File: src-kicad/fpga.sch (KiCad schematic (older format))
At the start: 1 part

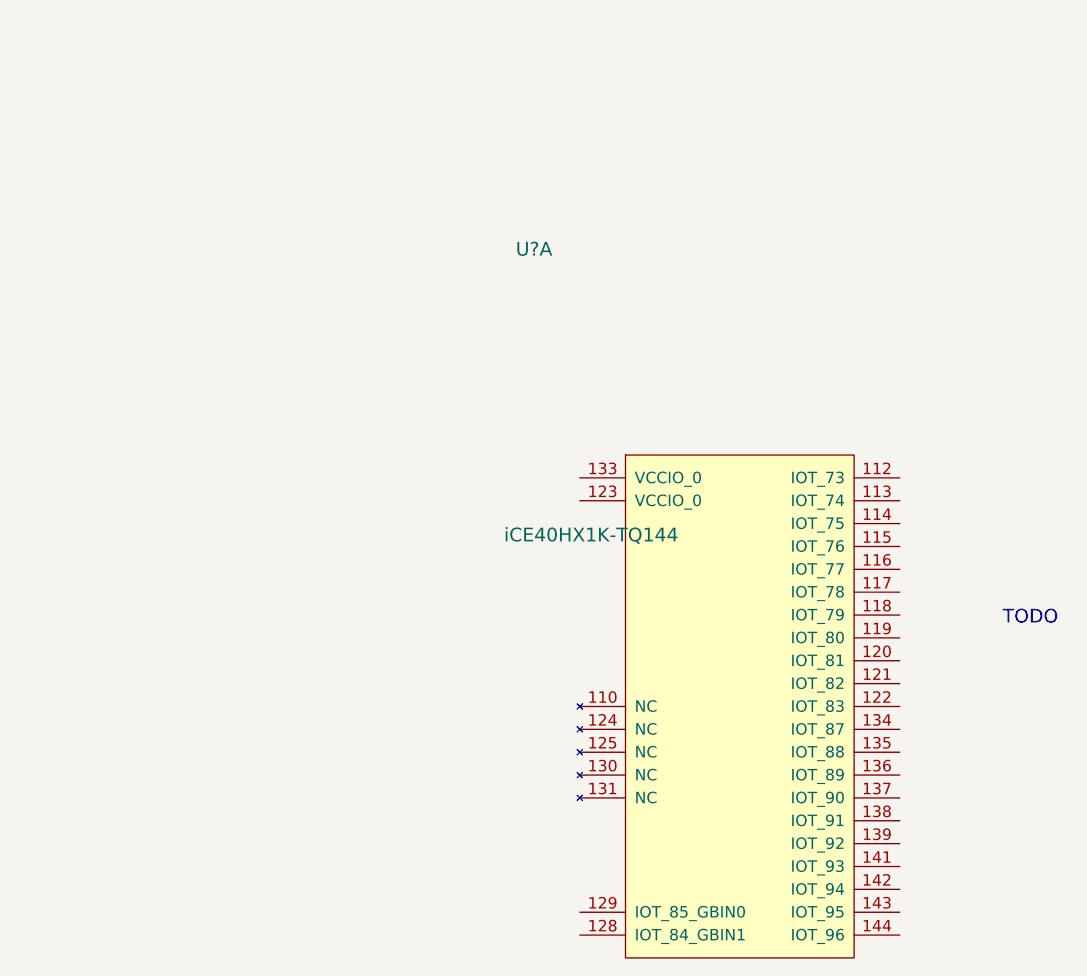
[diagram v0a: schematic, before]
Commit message: Kicad migration: component FPGA bank0 done
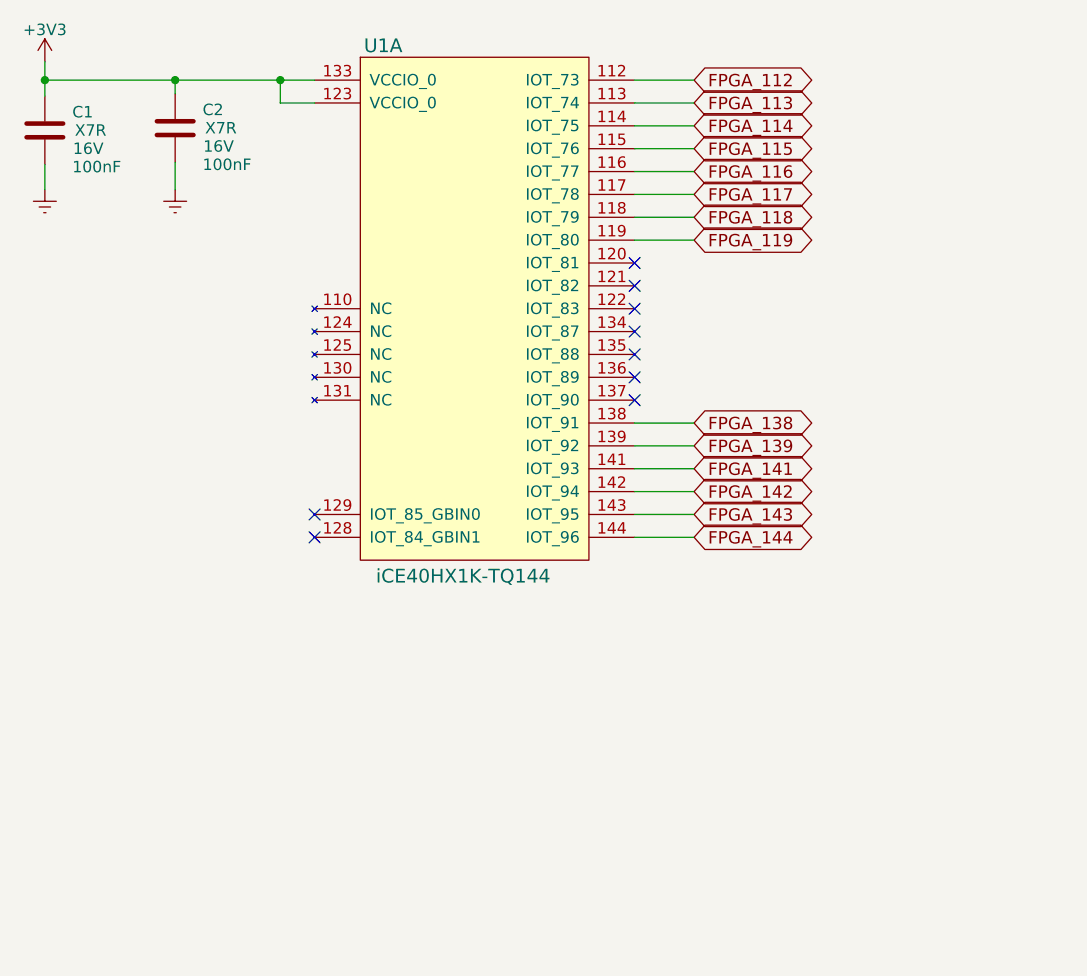
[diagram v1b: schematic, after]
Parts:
- removed U?: iCE40HX1K-TQ144, symbol iCE40HX1K-TQ144
- added C1, C2: 100nF, symbol C
- added U1: iCE40HX1K-TQ144, symbol iCE40HX1K-TQ144
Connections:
- new net +3V3: C1.1, C2.1, U1.123 (VCCIO_0), U1.133 (VCCIO_0)
- new net FPGA_112: U1.112 (IOT_73)
- new net FPGA_113: U1.113 (IOT_74)
- new net FPGA_114: U1.114 (IOT_75)
- new net FPGA_115: U1.115 (IOT_76)
- new net FPGA_116: U1.116 (IOT_77)
- new net FPGA_117: U1.117 (IOT_78)
- new net FPGA_118: U1.118 (IOT_79)
- new net FPGA_119: U1.119 (IOT_80)
- new net FPGA_138: U1.138 (IOT_91)
- new net FPGA_139: U1.139 (IOT_92)
- new net FPGA_141: U1.141 (IOT_93)
- new net FPGA_142: U1.142 (IOT_94)
- new net FPGA_143: U1.143 (IOT_95)
- new net FPGA_144: U1.144 (IOT_96)
- new net GNDREF: C1.2, C2.2
- no-connect marks 0 -> 9
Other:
- note removed: "TODO"
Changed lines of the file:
@@
 encoding utf-8
 Sheet 2 2
-Title ""
-Date ""
+Title "Icezum Alhambra"
+Date "2016-05-23"
 Rev ""
 Comp ""
@@
 Comment4 ""
 $EndDescr
-Text Notes 5150 3400 0    60   ~ 0
-TODO
 $Comp
-L iCE40HX1K-TQ144 U?
-U 1 1 5742AF05
-P 3300 2750
-F 0 "U?" H 3100 3750 60  0000 C CNN
-F 1 "iCE40HX1K-TQ144" H 3350 2500 60  0000 C CNN
-F 2 "" H 3300 2750 60  0000 C CNN
-F 3 "" H 3300 2750 60  0000 C CNN
-	1    3300 2750
+L iCE40HX1K-TQ144 U1
+U 1 1 5742DE36
+P 2140 1010
+F 0 "U1" H 2440 1160 60  0000 C CNN
+F 1 "iCE40HX1K-TQ144" H 2790 -1160 60  0000 C CNN
+F 2 "" H 2440 610 60  0000 C CNN
+F 3 "" H 2440 610 60  0000 C CNN
+	1    2140 1010
 	1    0    0    -1
 $EndComp
+$Comp
+L C C1
+U 1 1 5742E2A9
+P 960 1230
+F 0 "C1" H 1080 1310 50  0000 L CNN
+F 1 "100nF" H 1080 1070 50  0000 L CNN
+F 2 "" H 998 1080 50  0000 C CNN
+F 3 "" H 960 1230 50  0000 C CNN
+F 4 "X7R" H 1160 1230 50  0000 C CNN "class"
+F 5 "16V" H 1150 1150 50  0000 C CNN "Voltage"
+	1    960  1230
+	1    0    0    -1
+$EndComp
+$Comp
+L +3V3 #PWR?
+U 1 1 5742EB21
+P 960 930
+F 0 "#PWR?" H 960 780 50  0001 C CNN
+F 1 "+3V3" H 960 1070 50  0000 C CNN
+F 2 "" H 960 930 50  0000 C CNN
+F 3 "" H 960 930 50  0000 C CNN
+	1    960  930
+	1    0    0    -1
+$EndComp
+Wire Wire Line
+	960  930  960  1080
+$Comp
+L GNDREF #PWR?
+U 1 1 5742F120
+P 960 1490
+F 0 "#PWR?" H 960 1240 50  0001 C CNN
+F 1 "GNDREF" H 960 1340 50  0001 C CNN
+F 2 "" H 960 1490 50  0000 C CNN
+F 3 "" H 960 1490 50  0000 C CNN
+	1    960  1490
+	1    0    0    -1
+$EndComp
+Wire Wire Line
+	960  1490 960  1380
+$Comp
+L C C2
+U 1 1 5742F27A
+P 1530 1220
+F 0 "C2" H 1650 1300 50  0000 L CNN
+F 1 "100nF" H 1650 1060 50  0000 L CNN
+F 2 "" H 1568 1070 50  0000 C CNN
+F 3 "" H 1530 1220 50  0000 C CNN
+F 4 "X7R" H 1730 1220 50  0000 C CNN "class"
+F 5 "16V" H 1720 1140 50  0000 C CNN "Voltage"
+	1    1530 1220
+	1    0    0    -1
+$EndComp
+$Comp
+L GNDREF #PWR?
+U 1 1 5742F317
+P 1530 1490
+F 0 "#PWR?" H 1530 1240 50  0001 C CNN
+F 1 "GNDREF" H 1530 1340 50  0001 C CNN
+F 2 "" H 1530 1490 50  0000 C CNN
+F 3 "" H 1530 1490 50  0000 C CNN
+	1    1530 1490
+	1    0    0    -1
+$EndComp
+Wire Wire Line
+	1530 1370 1530 1490
+Wire Wire Line
+	960  1010 2140 1010
+Connection ~ 960  1010
+Wire Wire Line
+	1530 1070 1530 1010
+Connection ~ 1530 1010
+Wire Wire Line
+	2140 1110 1990 1110
+Wire Wire Line
+	1990 1110 1990 1010
+Connection ~ 1990 1010
+NoConn ~ 2140 2910
+NoConn ~ 2140 3010
+Wire Wire Line
+	3540 1010 3800 1010
+Text GLabel 3800 1010 2    54   BiDi ~ 0
+FPGA_112
+Text GLabel 3800 1110 2    54   BiDi ~ 0
+FPGA_113
+Wire Wire Line
+	3540 1110 3800 1110
+Text GLabel 3800 1210 2    54   BiDi ~ 0
+FPGA_114
+Text GLabel 3800 1310 2    54   BiDi ~ 0
+FPGA_115
+Text GLabel 3800 1410 2    54   BiDi ~ 0
+FPGA_116
+Text GLabel 3800 1510 2    54   BiDi ~ 0
+FPGA_117
+Text GLabel 3800 1610 2    54   BiDi ~ 0
+FPGA_118
+Text GLabel 3800 1710 2    54   BiDi ~ 0
+FPGA_119
+Wire Wire Line
+	3540 1210 3800 1210
+Wire Wire Line
+	3800 1310 3540 1310
+Wire Wire Line
+	3540 1410 3800 1410
+Wire Wire Line
+	3800 1510 3540 1510
+Wire Wire Line
+	3540 1610 3800 1610
+Wire Wire Line
+	3800 1710 3540 1710
+Text GLabel 3800 2510 2    54   BiDi ~ 0
+FPGA_138
+Text GLabel 3800 2610 2    54   BiDi ~ 0
+FPGA_139
+Text GLabel 3800 2710 2    54   BiDi ~ 0
+FPGA_141
+Text GLabel 3800 2810 2    54   BiDi ~ 0
+FPGA_142
+Text GLabel 3800 2910 2    54   BiDi ~ 0
+FPGA_143
+Text GLabel 3800 3010 2    54   BiDi ~ 0
+FPGA_144
+Wire Wire Line
+	3540 3010 3800 3010
+Wire Wire Line
+	3800 2910 3540 2910
+Wire Wire Line
+	3540 2810 3800 2810
+Wire Wire Line
+	3800 2710 3540 2710
+Wire Wire Line
+	3540 2610 3800 2610
+Wire Wire Line
+	3540 2510 3800 2510
+NoConn ~ 3540 1810
+NoConn ~ 3540 1910
+NoConn ~ 3540 2010
+NoConn ~ 3540 2110
+NoConn ~ 3540 2210
+NoConn ~ 3540 2310
+NoConn ~ 3540 2410
 $EndSCHEMATC

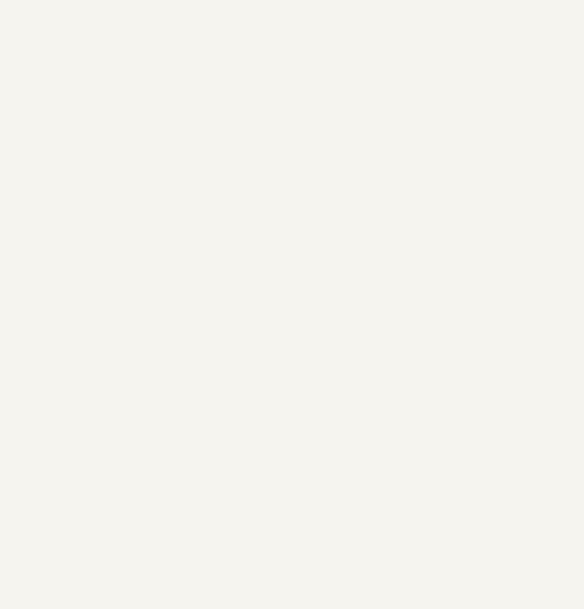
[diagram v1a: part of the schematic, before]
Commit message: Kicad. FPGA: bank 1 component created
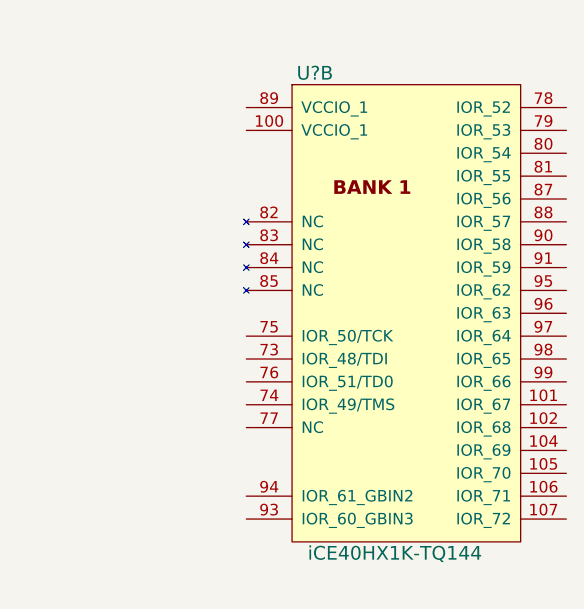
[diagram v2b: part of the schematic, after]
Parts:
- added U?: iCE40HX1K-TQ144, symbol iCE40HX1K-TQ144
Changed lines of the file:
@@
 NoConn ~ 3540 2310
 NoConn ~ 3540 2410
+$Comp
+L iCE40HX1K-TQ144 U?
+U 2 1 57436BD0
+P 5700 1130
+F 0 "U?" H 6000 1280 60  0000 C CNN
+F 1 "iCE40HX1K-TQ144" H 6350 -820 60  0000 C CNN
+F 2 "" H 6000 730 60  0000 C CNN
+F 3 "" H 6000 730 60  0000 C CNN
+	2    5700 1130
+	1    0    0    -1
+$EndComp
 $EndSCHEMATC
